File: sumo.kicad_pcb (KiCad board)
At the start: 2 copper layers, 76.2 x 94 mm, 57 parts, among them Q1 BPW40, Q2 BPW40, SW1 SW_Push, SW2 SW_DIP_x01, SW3 SW_DIP_x01, SW4 SW_DIP_x01, SW5 SW_DIP_x01, T1 Screw_Terminal_01x04, T2 Screw_Terminal_01x05, T3 Screw_Terminal_01x04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

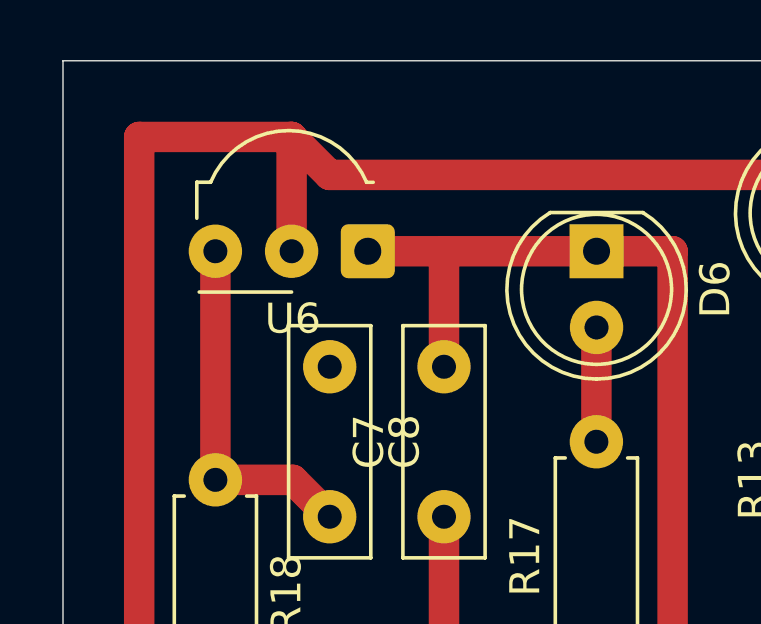
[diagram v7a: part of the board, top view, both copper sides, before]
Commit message: some value fixes
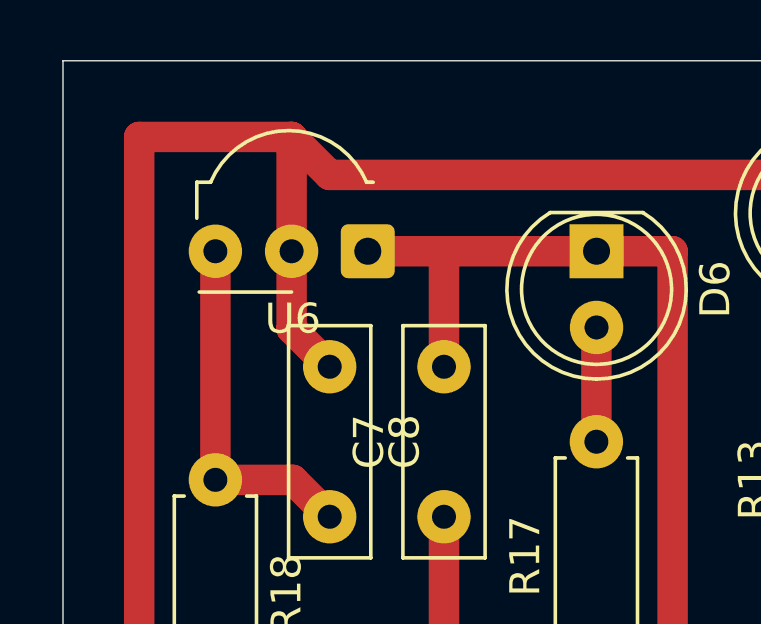
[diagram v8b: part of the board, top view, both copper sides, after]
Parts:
- R13, R4, R8: value 230 -> 220
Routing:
- net GNDREF: track 370.3 -> 374.7 mm
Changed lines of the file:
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@@
 			)
 		)
-		(property "Value" "230"
+		(property "Value" "220"
 			(at 3.81 2.37 90)
 			(layer "F.Fab")
@@
 			)
 		)
-		(property "Value" "230"
+		(property "Value" "220"
 			(at 3.81 2.37 -90)
 			(layer "F.Fab")
@@
 			)
 		)
-		(property "Value" "230"
+		(property "Value" "220"
 			(at 3.81 2.37 -90)
 			(layer "F.Fab")
@@
 	)
 	(segment
+		(start 134.62 47.03)
+		(end 134.62 44.45)
+		(width 1.016)
+		(layer "F.Cu")
+		(net 4)
+	)
+	(segment
 		(start 179.0954 87.6046)
 		(end 138.4046 87.6046)
@@
 		(width 1.016)
 		(layer "F.Cu")
+		(net 4)
+	)
+	(segment
+		(start 135.89 48.3)
+		(end 134.62 47.03)
+		(width 1.016)
+		(layer "F.Cu")
